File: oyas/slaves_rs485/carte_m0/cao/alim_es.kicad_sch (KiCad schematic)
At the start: 50 parts, among them J1 POWER, U1 BPC_Alim5V, U1 MAX3485, U4 AP1117-15

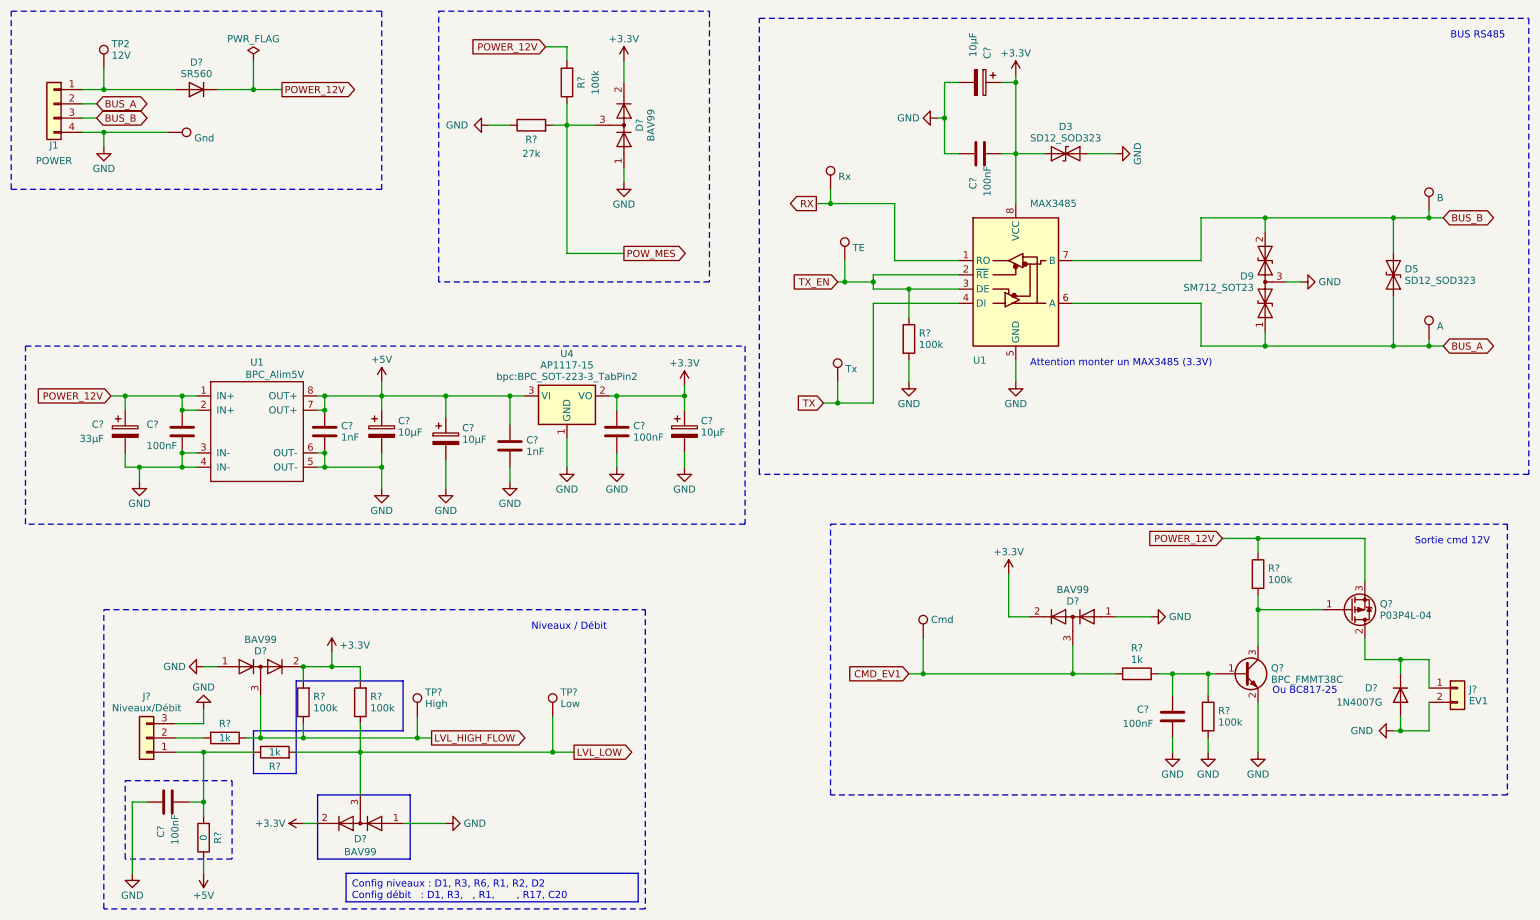
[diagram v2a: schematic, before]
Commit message: Fin de revue avec ajout d'une diode TVS 18V en entrée
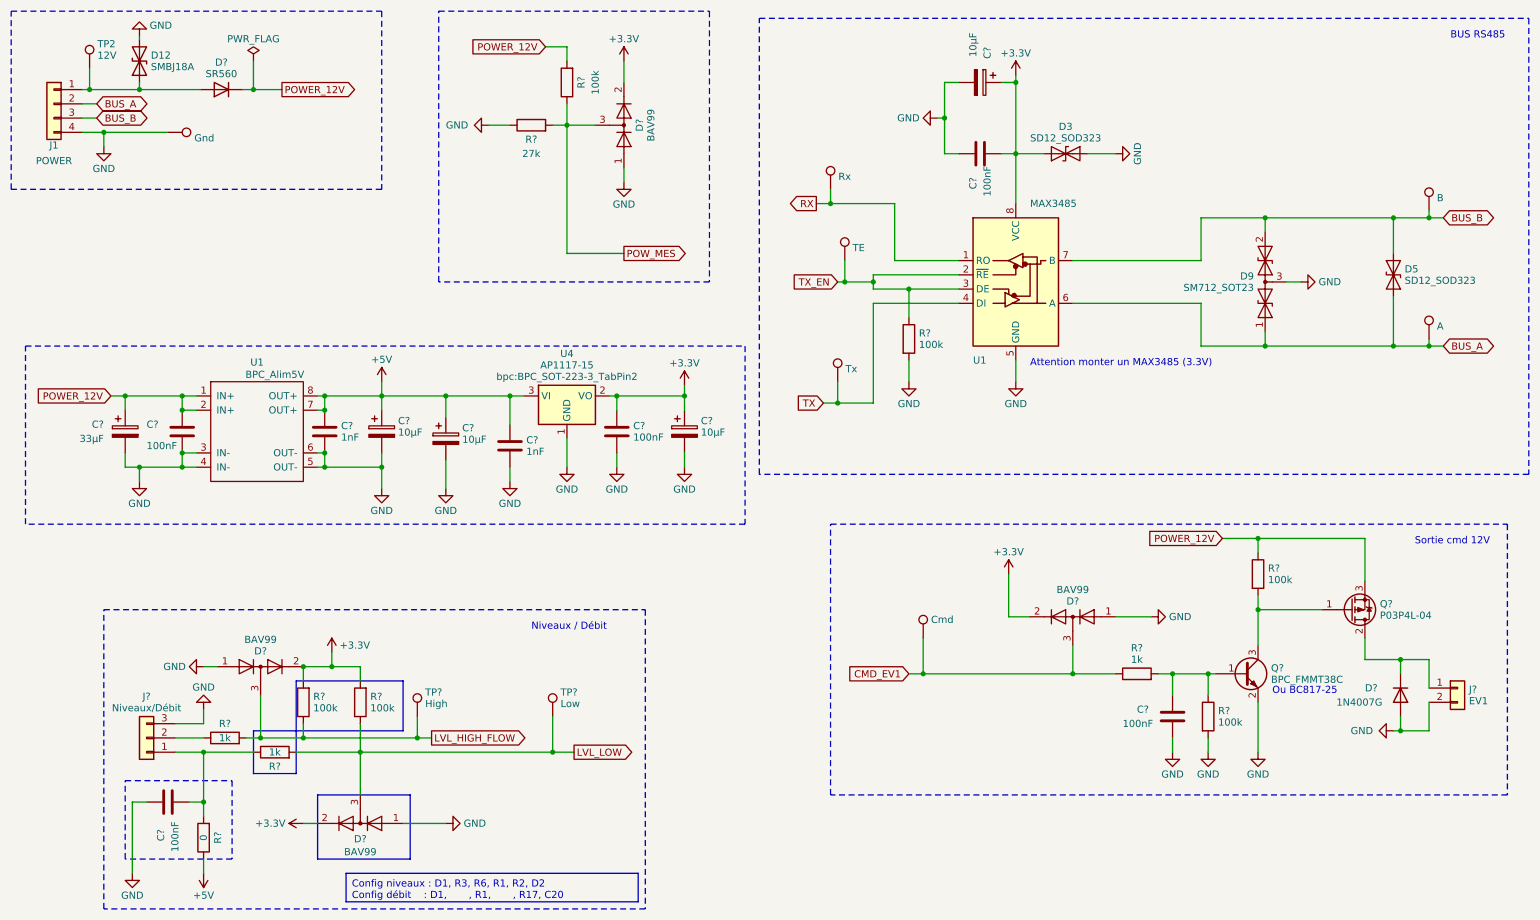
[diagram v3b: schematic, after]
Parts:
- added D12: SMBJ18A, Diode_SMD:D_SMB_Handsoldering, symbol Device:D_TVS
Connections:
- net GND: now also D12.2 (A2)
- net at D?.2 (A), J1.1 (Pin_1), TP2.1: now also D12.1 (A1)
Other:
- title: Carte Oya M0 -> Esclave Oya M0
- moved on the sheet: D?, TP2
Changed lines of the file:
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@@
   (paper "A4")
   (title_block
-    (title "Carte Oya M0")
-    (date "2026-03-06")
-    (rev "Rev A")
+    (title "Esclave Oya M0")
+    (date "2026-03-07")
+    (rev "A")
     (company "BPC")
+    (comment 1 "Technologie avec M0 / Petite carte")
+    (comment 2 "Monitoring de tension d'alimentation")
+    (comment 3 "1 sortie 12V/5A - 2 entrées TOR (niveaux) ou 1 débimètre - 1 LED - RS485")
   )
   (junction (at 179.07 34.29) (diameter 0) (color 0 0 0 0)
@@
   (junction (at 78.74 96.52) (diameter 0) (color 0 0 0 0)
   )
+  (junction (at 26.67 29.21) (diameter 0) (color 0 0 0 0)
+  )
   (junction (at 43.18 96.52) (diameter 0) (color 0 0 0 0)
   )
@@
   (junction (at 219.71 133.35) (diameter 0) (color 0 0 0 0)
   )
+  (junction (at 35.56 29.21) (diameter 0) (color 0 0 0 0)
+  )
   (junction (at 120.65 83.82) (diameter 0) (color 0 0 0 0)
   )
@@
   (junction (at 259.08 52.07) (diameter 0) (color 0 0 0 0)
   )
-  (junction (at 29.21 29.21) (diameter 0) (color 0 0 0 0)
-  )
   (junction (at 172.72 64.77) (diameter 0) (color 0 0 0 0)
   )
@@
     (stroke (width 0) (type default))
   )
+  (wire (pts (xy 35.56 29.21) (xy 46.355 29.21))
+    (stroke (width 0) (type default))
+  )
   (wire (pts (xy 179.07 40.64) (xy 179.07 34.29))
     (stroke (width 0) (type default))
@@
     (stroke (width 0) (type default))
   )
-  (wire (pts (xy 29.21 25.4) (xy 29.21 29.21))
+  (wire (pts (xy 26.67 25.4) (xy 26.67 29.21))
     (stroke (width 0) (type default))
   )
@@
     (stroke (width 0) (type default))
   )
+  (wire (pts (xy 35.56 19.685) (xy 35.56 20.32))
+    (stroke (width 0) (type default))
+  )
   (wire (pts (xy 236.22 74.93) (xy 224.79 74.93))
     (stroke (width 0) (type default))
@@
     (stroke (width 0) (type default))
   )
+  (wire (pts (xy 35.56 27.94) (xy 35.56 29.21))
+    (stroke (width 0) (type default))
+  )
   (wire (pts (xy 43.18 83.82) (xy 45.72 83.82))
     (stroke (width 0) (type default))
@@
     (stroke (width 0) (type default))
   )
-  (wire (pts (xy 29.21 29.21) (xy 41.91 29.21))
+  (wire (pts (xy 26.67 29.21) (xy 35.56 29.21))
     (stroke (width 0) (type default))
   )
@@
     (stroke (width 0) (type default))
   )
-  (wire (pts (xy 49.53 29.21) (xy 55.88 29.21))
+  (wire (pts (xy 53.975 29.21) (xy 55.88 29.21))
     (stroke (width 0) (type default))
   )
@@
     (stroke (width 0) (type default))
   )
-  (wire (pts (xy 25.4 29.21) (xy 29.21 29.21))
+  (wire (pts (xy 25.4 29.21) (xy 26.67 29.21))
     (stroke (width 0) (type default))
   )
@@
     (fill (type none))
   )
-  (text_box "Config niveaux : D1, R3, R6, R1, R2, D2\nConfig débit   : D1, R3,   , R1,       , R17, C20 "
+  (text_box "Config niveaux : D1, R3, R6, R1, R2, D2\nConfig débit    : D1,       , R1,       , R17, C20 "
     (at 72.39 168.91 0) (size 52.07 5.08)
     (stroke (width 0) (type default))
@@
     )
   )
-  (symbol (lib_id "Device:D") (at 45.72 29.21 180) (unit 1)
+  (symbol (lib_id "Device:D") (at 50.165 29.21 180) (unit 1)
     (in_bom yes) (on_board yes) (dnp no) (fields_autoplaced)
-    (property "Reference" "D?" (at 45.72 24.36 0)
+    (property "Reference" "D?" (at 50.165 24.36 0)
       (effects (font (size 1.27 1.27)))
     )
-    (property "Value" "SR560" (at 45.72 26.408 0)
+    (property "Value" "SR560" (at 50.165 26.408 0)
       (effects (font (size 1.27 1.27)))
     )
-    (property "Footprint" "Diode_THT:D_DO-15_P12.70mm_Horizontal" (at 45.72 29.21 0)
+    (property "Footprint" "Diode_THT:D_DO-15_P12.70mm_Horizontal" (at 50.165 29.21 0)
       (effects (font (size 1.27 1.27)) hide)
     )
-    (property "Datasheet" "~" (at 45.72 29.21 0)
+    (property "Datasheet" "~" (at 50.165 29.21 0)
       (effects (font (size 1.27 1.27)) hide)
     )
-    (property "Sim.Device" "D" (at 45.72 29.21 0)
+    (property "Sim.Device" "D" (at 50.165 29.21 0)
       (effects (font (size 1.27 1.27)) hide)
     )
-    (property "Sim.Pins" "1=K 2=A" (at 45.72 29.21 0)
+    (property "Sim.Pins" "1=K 2=A" (at 50.165 29.21 0)
       (effects (font (size 1.27 1.27)) hide)
     )
-    (property "RefFabricant" "SR560" (at 45.72 29.21 0)
+    (property "RefFabricant" "SR560" (at 50.165 29.21 0)
       (effects (font (size 1.27 1.27)) hide)
     )
-    (property "RefFournisseur" "2675411" (at 45.72 29.21 0)
+    (property "RefFournisseur" "2675411" (at 50.165 29.21 0)
       (effects (font (size 1.27 1.27)) hide)
     )
-    (property "Fabricant" "MULTICOMP PRO" (at 45.72 29.21 0)
+    (property "Fabricant" "MULTICOMP PRO" (at 50.165 29.21 0)
       (effects (font (size 1.27 1.27)) hide)
     )
-    (property "Fournisseur" "Farnell" (at 45.72 29.21 0)
+    (property "Fournisseur" "Farnell" (at 50.165 29.21 0)
       (effects (font (size 1.27 1.27)) hide)
     )
-    (property "Description" "Diode de redressement SR560" (at 45.72 29.21 0)
+    (property "Description" "Diode de redressement SR560" (at 50.165 29.21 0)
       (effects (font (size 1.27 1.27)) hide)
     )
-    (property "Price" "0,5844" (at 45.72 29.21 0)
+    (property "Price" "0,5844" (at 50.165 29.21 0)
       (effects (font (size 1.27 1.27)) hide)
     )
@@
     )
   )
-  (symbol (lib_id "Connector:TestPoint") (at 29.21 25.4 0) (unit 1)
+  (symbol (lib_id "Connector:TestPoint") (at 26.67 25.4 0) (unit 1)
     (in_bom yes) (on_board yes) (dnp no) (fields_autoplaced)
-    (property "Reference" "TP2" (at 30.607 21.074 0)
+    (property "Reference" "TP2" (at 28.067 21.074 0)
       (effects (font (size 1.27 1.27)) (justify left))
     )
-    (property "Value" "12V" (at 30.607 23.122 0)
+    (property "Value" "12V" (at 28.067 23.122 0)
       (effects (font (size 1.27 1.27)) (justify left))
     )
-    (property "Footprint" "TestPoint:TestPoint_Pad_D1.0mm" (at 34.29 25.4 0)
+    (property "Footprint" "TestPoint:TestPoint_Pad_D1.0mm" (at 31.75 25.4 0)
       (effects (font (size 1.27 1.27)) hide)
     )
-    (property "Datasheet" "~" (at 34.29 25.4 0)
+    (property "Datasheet" "~" (at 31.75 25.4 0)
       (effects (font (size 1.27 1.27)) hide)
     )
-    (property "RefFabricant" "" (at 29.21 25.4 0)
+    (property "RefFabricant" "" (at 26.67 25.4 0)
       (effects (font (size 1.27 1.27)) hide)
     )
-    (property "RefFournisseur" "" (at 29.21 25.4 0)
+    (property "RefFournisseur" "" (at 26.67 25.4 0)
       (effects (font (size 1.27 1.27)) hide)
     )
-    (property "Price" "0" (at 29.21 25.4 0)
+    (property "Price" "0" (at 26.67 25.4 0)
       (effects (font (size 1.27 1.27)) hide)
     )
@@
     )
   )
+  (symbol (lib_id "power:GND") (at 35.56 19.685 180) (unit 1)
+    (in_bom yes) (on_board yes) (dnp no)
+    (property "Reference" "#PWR?" (at 35.56 13.335 0)
+      (effects (font (size 1.27 1.27)) hide)
+    )
+    (property "Value" "GND" (at 39.37 17.78 0)
+      (effects (font (size 1.27 1.27)))
+    )
+    (property "Footprint" "" (at 35.56 19.685 0)
+      (effects (font (size 1.27 1.27)) hide)
+    )
+    (property "Datasheet" "" (at 35.56 19.685 0)
+      (effects (font (size 1.27 1.27)) hide)
+    )
+    (pin "1")
+    (instances
+      (project "jard_rs485_slave_mods2"
+        (path "/5ae93d62-0543-4c0e-b37d-d67af6219e1b"
+          (reference "#PWR?") (unit 1)
+        )
+        (path "/5ae93d62-0543-4c0e-b37d-d67af6219e1b/36e9fbeb-2032-4e73-95af-53e316cf916d"
+          (reference "#PWR01") (unit 1)
+        )
+      )
+      (project "jard_rs485_slave_m0"
+        (path "/a198b99e-c4dc-4064-b4d8-b20710c7a061"
+          (reference "#PWR013") (unit 1)
+        )
+        (path "/a198b99e-c4dc-4064-b4d8-b20710c7a061/fab97b7a-d6f8-430d-b29e-f9e08ccfedcc"
+          (reference "#PWR052") (unit 1)
+        )
+      )
+    )
+  )
   (symbol (lib_id "Device:R") (at 74.93 138.43 180) (unit 1)
     (in_bom yes) (on_board yes) (dnp no) (fields_autoplaced)
@@
     )
   )
+  (symbol (lib_id "Device:D_TVS") (at 35.56 24.13 90) (unit 1)
+    (in_bom yes) (on_board yes) (dnp no) (fields_autoplaced)
+    (property "Reference" "D12" (at 37.592 23.106 90)
+      (effects (font (size 1.27 1.27)) (justify right))
+    )
+    (property "Value" "SMBJ18A" (at 37.592 25.154 90)
+      (effects (font (size 1.27 1.27)) (justify right))
+    )
+    (property "Footprint" "Diode_SMD:D_SMB_Handsoldering" (at 35.56 24.13 0)
+      (effects (font (size 1.27 1.27)) hide)
+    )
+    (property "Datasheet" "~" (at 35.56 24.13 0)
+      (effects (font (size 1.27 1.27)) hide)
+    )
+    (pin "1")
+    (pin "2")
+    (instances
+      (project "jard_rs485_slave_m0"
+        (path "/a198b99e-c4dc-4064-b4d8-b20710c7a061/fab97b7a-d6f8-430d-b29e-f9e08ccfedcc"
+          (reference "D12") (unit 1)
+        )
+      )
+    )
+  )
   (symbol (lib_id "Connector:TestPoint") (at 85.09 140.97 0) (unit 1)
     (in_bom yes) (on_board yes) (dnp no) (fields_autoplaced)
@@
   (symbol (lib_id "Device:C") (at 40.64 156.21 90) (unit 1)
     (in_bom yes) (on_board yes) (dnp no)
-    (property "Reference" "C?" (at 39.37 162.56 0)
+    (property "Reference" "C?" (at 39.37 163.195 0)
       (effects (font (size 1.27 1.27)) (justify left))
     )
-    (property "Value" "100nF" (at 41.91 163.83 0)
+    (property "Value" "100nF" (at 41.91 165.1 0)
       (effects (font (size 1.27 1.27)) (justify left))
     )

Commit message: Finalisation Future Rev B
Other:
- title: Esclave Oya M0 -> Esclave Oya m0
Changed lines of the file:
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@@
   (paper "A4")
   (title_block
-    (title "Esclave Oya M0")
-    (date "2026-04-14")
+    (title "Esclave Oya m0")
+    (date "2026-05-13")
     (rev "B")
     (company "BPC")
